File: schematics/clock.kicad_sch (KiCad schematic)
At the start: 5 parts, among them U3 UPD4990AC, X1 32.768KHz

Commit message: WIP
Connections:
- net BATYCC renamed BAT_VCC
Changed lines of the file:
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@@
     )
   )
-  (global_label "BATYCC" (shape input) (at 41.91 39.37 180) (fields_autoplaced)
+  (global_label "BAT_VCC" (shape input) (at 41.91 39.37 180) (fields_autoplaced)
     (effects (font (size 1.27 1.27)) (justify right))
     (property "Intersheetrefs" "${INTERSHEET_REFS}" (at 31.97 39.37 0)

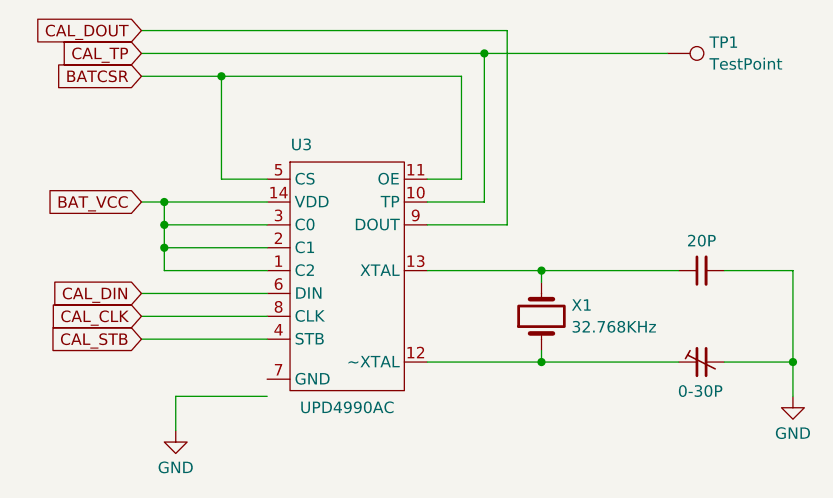
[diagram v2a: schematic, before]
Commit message: update "main" schematics
Adding LSPC2-A2, NEO-B1, L0 ROM
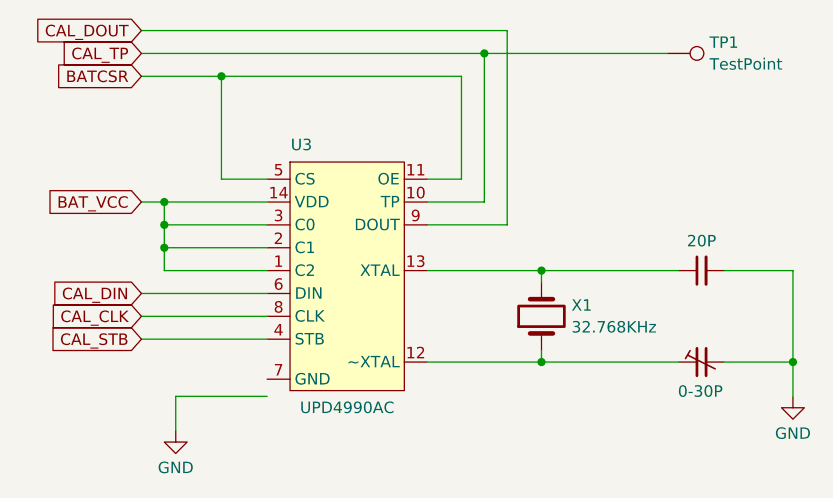
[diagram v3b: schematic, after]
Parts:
- U3: symbol 0-Custom-Frater_Library:UPD4990AC -> 0-Custom-SNK:UPD4990AC
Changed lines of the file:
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@@
     )
   )
-  (symbol (lib_id "0-Custom-Frater_Library:UPD4990AC") (at 64.77 46.99 0) (unit 1)
+  (symbol (lib_id "0-Custom-SNK:UPD4990AC") (at 64.77 46.99 0) (unit 1)
     (in_bom yes) (on_board yes) (dnp no)
     (property "Reference" "U3" (at 59.69 33.02 0)
@@
       (effects (font (size 1.27 1.27)))
     )
-    (property "Footprint" "Package_DIP:DIP-14_W7.62mm" (at 34.29 46.99 0)
+    (property "Footprint" "Package_DIP:DIP-14_W7.62mm" (at 65.405 27.305 0)
       (effects (font (size 1.27 1.27)) hide)
     )
-    (property "Datasheet" "https://pdf1.alldatasheet.com/datasheet-pdf/download/6956/NEC/UPD4990AC.html" (at 83.82 46.99 0)
+    (property "Datasheet" "https://pdf1.alldatasheet.com/datasheet-pdf/download/6956/NEC/UPD4990AC.html" (at 74.295 67.945 0)
       (effects (font (size 1.27 1.27)) hide)
     )

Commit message: Audio Amp + player's button LED & marquee + Coins Up + 45% raiser card connectors
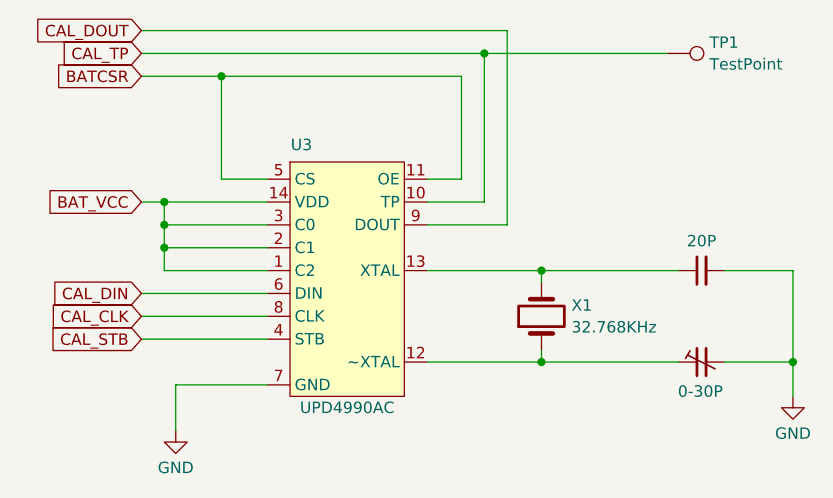
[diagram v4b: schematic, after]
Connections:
- net GND: now also U3.7 (GND)
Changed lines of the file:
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@@
+    (stroke (width 0) (type default))
+  )
+  (wire (pts (xy 45.72 59.69) (xy 45.72 64.77))
     (stroke (width 0) (type default))
   )
@@
   )
   (wire (pts (xy 86.36 57.15) (xy 73.66 57.15))
-    (stroke (width 0) (type default))
-  )
-  (wire (pts (xy 45.72 64.77) (xy 45.72 60.96))
     (stroke (width 0) (type default))
   )
@@
     (stroke (width 0) (type default))
   )
-  (wire (pts (xy 45.72 60.96) (xy 55.88 60.96))
+  (wire (pts (xy 45.72 59.69) (xy 55.88 59.69))
     (stroke (width 0) (type default))
   )
